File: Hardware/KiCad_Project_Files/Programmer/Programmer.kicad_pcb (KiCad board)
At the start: 2 copper layers, 85 x 56 mm, 24 parts, among them J1 USB_C_Receptacle_USB2.0, J2 R_PI_4, J3 SWD, Q1 FDN335N, U1 MIC5205-3.3YM5, U2 ATSAMD21G18A-A, Y1 32.876

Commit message: layout init
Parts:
- C3, C4, C5, C6, C7, C8, C9, R2, R3, R4, R5, Y1: moved to B.Cu
- moved C1 103.9 mm to (20.0, 40.0), turned to -90 degrees
- moved R3 98.4 mm to (21.5, 32.8), turned to -90 degrees
- moved C3 96.4 mm to (31.5, 44.5)
- moved R2 92.6 mm to (21.5, 25.2), turned to 90 degrees
- moved C4 90.4 mm to (29.5, 47.5), turned to -90 degrees
- moved C2 89.2 mm to (26.0, 40.0), turned to -90 degrees
- moved R1 86.8 mm to (20.0, 44.0), turned to -90 degrees
- moved C6 80.0 mm to (45.5, 51.5), turned to -90 degrees
- moved C7 79.6 mm to (31.5, 51.5), turned to 90 degrees
- moved C9 75.9 mm to (40.0, 45.5)
- moved R4 71.6 mm to (45.0, 65.5), turned to -90 degrees
- moved C8 69.0 mm to (38.5, 59.5)
- moved D1 68.3 mm to (47.0, 65.5), turned to -90 degrees
- moved R5 66.9 mm to (51.0, 65.5), turned to -90 degrees
- moved D2 60.3 mm to (49.0, 65.5), turned to -90 degrees
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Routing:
- net /D-: track 0.00 -> 102.9 mm
- net /D+: track 0.00 -> 101.4 mm
- net Net-(J1-PadA5): track 0.00 -> 3.85 mm, vias 0 -> 1
- net Net-(J1-PadB5): track 0.00 -> 3.46 mm, vias 0 -> 1
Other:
- outline, holes or cut-outs redrawn

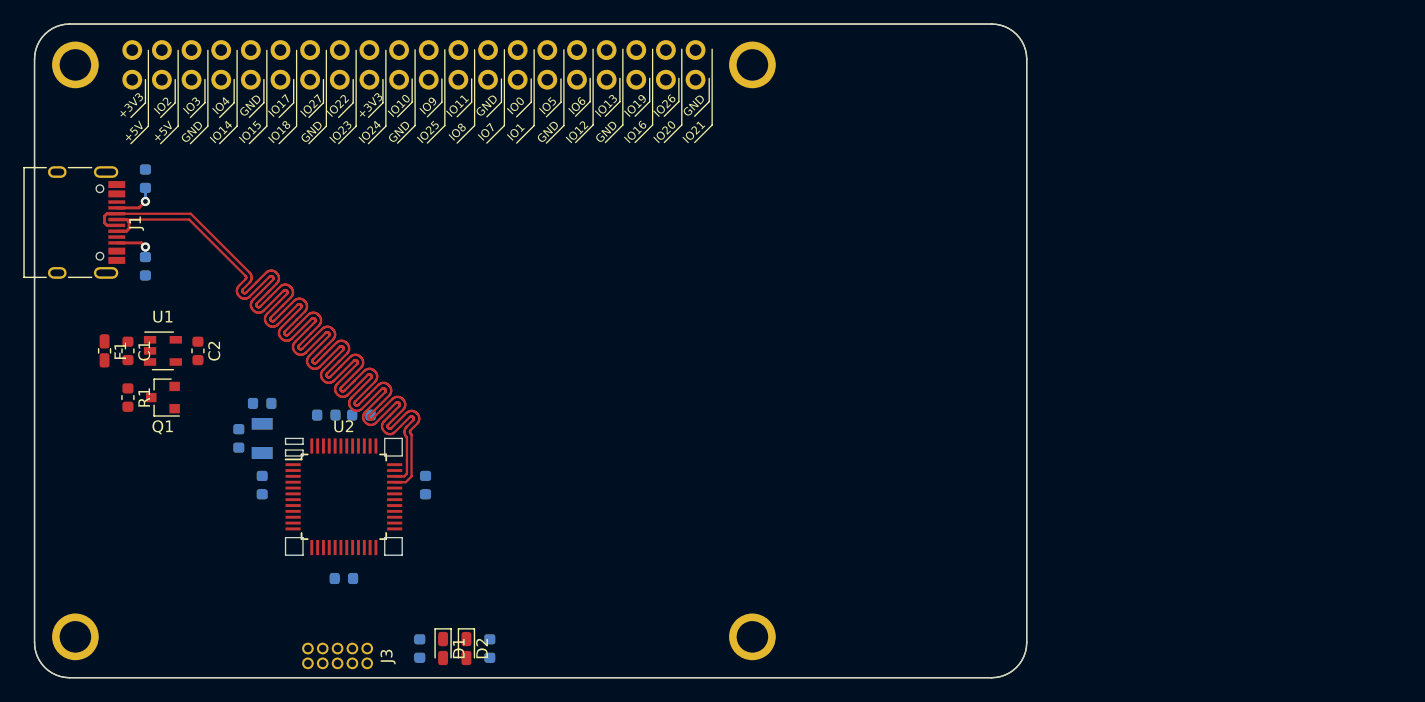
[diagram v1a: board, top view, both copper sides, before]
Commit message: added oled
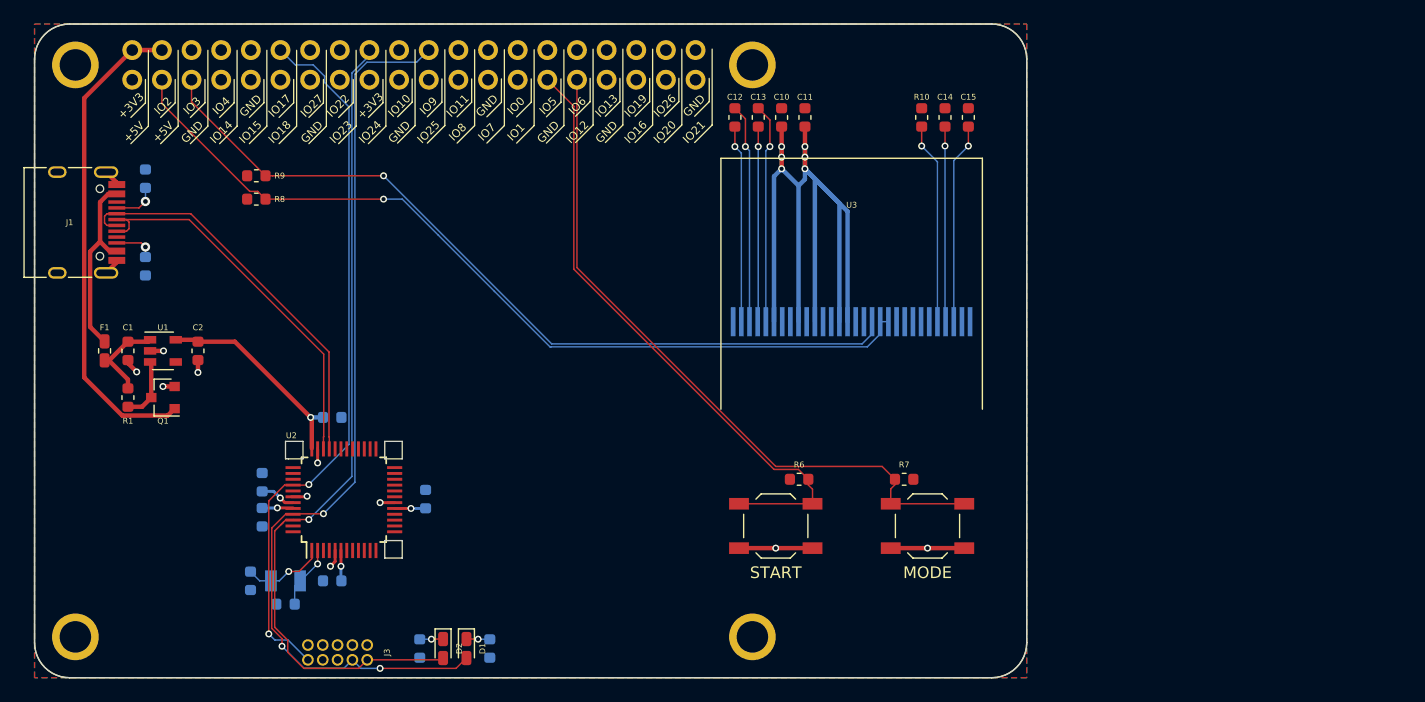
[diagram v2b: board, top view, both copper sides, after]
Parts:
- added C10: 1µF, Capacitor_SMD:C_0603_1608Metric, F.Cu at (76.0, 20.0)
- added C11: 1µF, Capacitor_SMD:C_0603_1608Metric, F.Cu at (78.0, 20.0)
- added C12: 1µF, Capacitor_SMD:C_0603_1608Metric, F.Cu at (72.0, 20.0)
- added C13: 1µF, Capacitor_SMD:C_0603_1608Metric, F.Cu at (74.0, 20.0)
- added C14: 4.7µF, Capacitor_SMD:C_0603_1608Metric, F.Cu at (90.0, 20.0)
- added C15: 2.2µF, Capacitor_SMD:C_0603_1608Metric, F.Cu at (92.0, 20.0)
- added R10: 5.1KΩ, Resistor_SMD:R_0603_1608Metric, F.Cu at (88.0, 20.0)
- added R6: 330Ω, Resistor_SMD:R_0603_1608Metric, F.Cu at (77.5, 51.0)
- added R7: 330Ω, Resistor_SMD:R_0603_1608Metric, F.Cu at (86.5, 51.0)
- added R8: 2.2KΩ, Resistor_SMD:R_0603_1608Metric, F.Cu at (31.0, 27.0)
- added R9: 2.2KΩ, Resistor_SMD:R_0603_1608Metric, F.Cu at (31.0, 25.0)
- added SW1: START, Button_Switch_SMD:SW_SPST_TL3342, F.Cu at (75.5, 55.0)
- added SW2: MODE, Button_Switch_SMD:SW_SPST_TL3342, F.Cu at (88.5, 55.0)
- added U3: SSD1306_0.96in, Custom_Displays:SSD1306_0.96in, F.Cu at (82.0, 34.0)
- moved C3 15.2 mm to (30.5, 59.7), turned to 90 degrees
- moved C4 14.8 mm to (33.5, 61.7), turned to 0 degrees
- moved Y1 12.4 mm to (33.5, 59.7), turned to 180 degrees
- moved C9 12.2 mm to (31.5, 54.2), turned to -90 degrees
- moved C7 10.2 mm to (37.5, 59.7), turned to 180 degrees
- moved C6 9.88 mm to (37.5, 45.7), turned to 0 degrees
- moved C8 9.76 mm to (45.5, 52.7), turned to 90 degrees
- moved C5 7.96 mm to (31.5, 51.2), turned to -90 degrees
- moved R4 6.00 mm to (51.0, 65.5)
- moved R5 6.00 mm to (45.0, 65.5)
- moved D1 2.00 mm to (49.0, 65.5)
- moved D2 2.00 mm to (47.0, 65.5)
- moved J3 0.30 mm to (40.5, 65.2)
- moved U2 0.25 mm to (38.5, 52.8), turned to 90 degrees
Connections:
- J2 pad 29: (no net) -> /START
- J2 pad 3: (no net) -> /SDA
- J2 pad 31: (no net) -> /MODE
- J2 pad 5: (no net) -> /SCL
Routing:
- net +3V3: track 0.00 -> 108.2 mm, vias 0 -> 10
- net /SWDCLK: track 0.00 -> 79.0 mm, vias 0 -> 3
- net /SDA: track 0.00 -> 74.4 mm, vias 0 -> 1
- net /SWDIO: track 0.00 -> 71.1 mm, vias 0 -> 1
- net /SCL: track 0.00 -> 70.2 mm, vias 0 -> 1
- net /D-: track 102.9 -> 34.2 mm
- net /D+: track 101.4 -> 33.4 mm
- net /~RST: track 0.00 -> 61.8 mm, vias 0 -> 2
- net /MODE: track 0.00 -> 59.4 mm
- net /START: track 0.00 -> 53.3 mm
- net +5V: track 0.00 -> 41.6 mm
- net GND: track 0.00 -> 25.5 mm, vias 0 -> 10
- net Net-(C13-Pad2): track 0.00 -> 18.8 mm, vias 0 -> 1
- net Net-(C12-Pad2): track 0.00 -> 18.8 mm, vias 0 -> 1
- net Net-(R10-Pad1): track 0.00 -> 17.3 mm, vias 0 -> 1
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- added copper zone on F.Cu, net +3V3
- added copper zone on B.Cu, net GND
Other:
- outline, holes or cut-outs redrawn

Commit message: layout complete
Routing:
- net GND: track 25.5 -> 34.0 mm, vias 10 -> 15
